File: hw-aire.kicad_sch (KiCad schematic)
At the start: 58 parts, among them J1 Conn_01x02_Pin, J2 Conn_01x02_Pin, J3 Screw_Terminal_01x12, J4 Conn_01x04_Pin, J5 Conn_01x05_Pin, K1 JRC-21F(4100), K2 JRC-21F(4100), K3 JRC-21F(4100), Q1 PMBT3904235, Q2 PMBT3904235, Q3 PMBT3904235, Q5 PMBT3904235, SW1 SW_Push, U1 HLK-2M05, U2 NCP1117-3.3_SOT223, U3 ESP-12E, U4 SHT4x, U5 BMP581

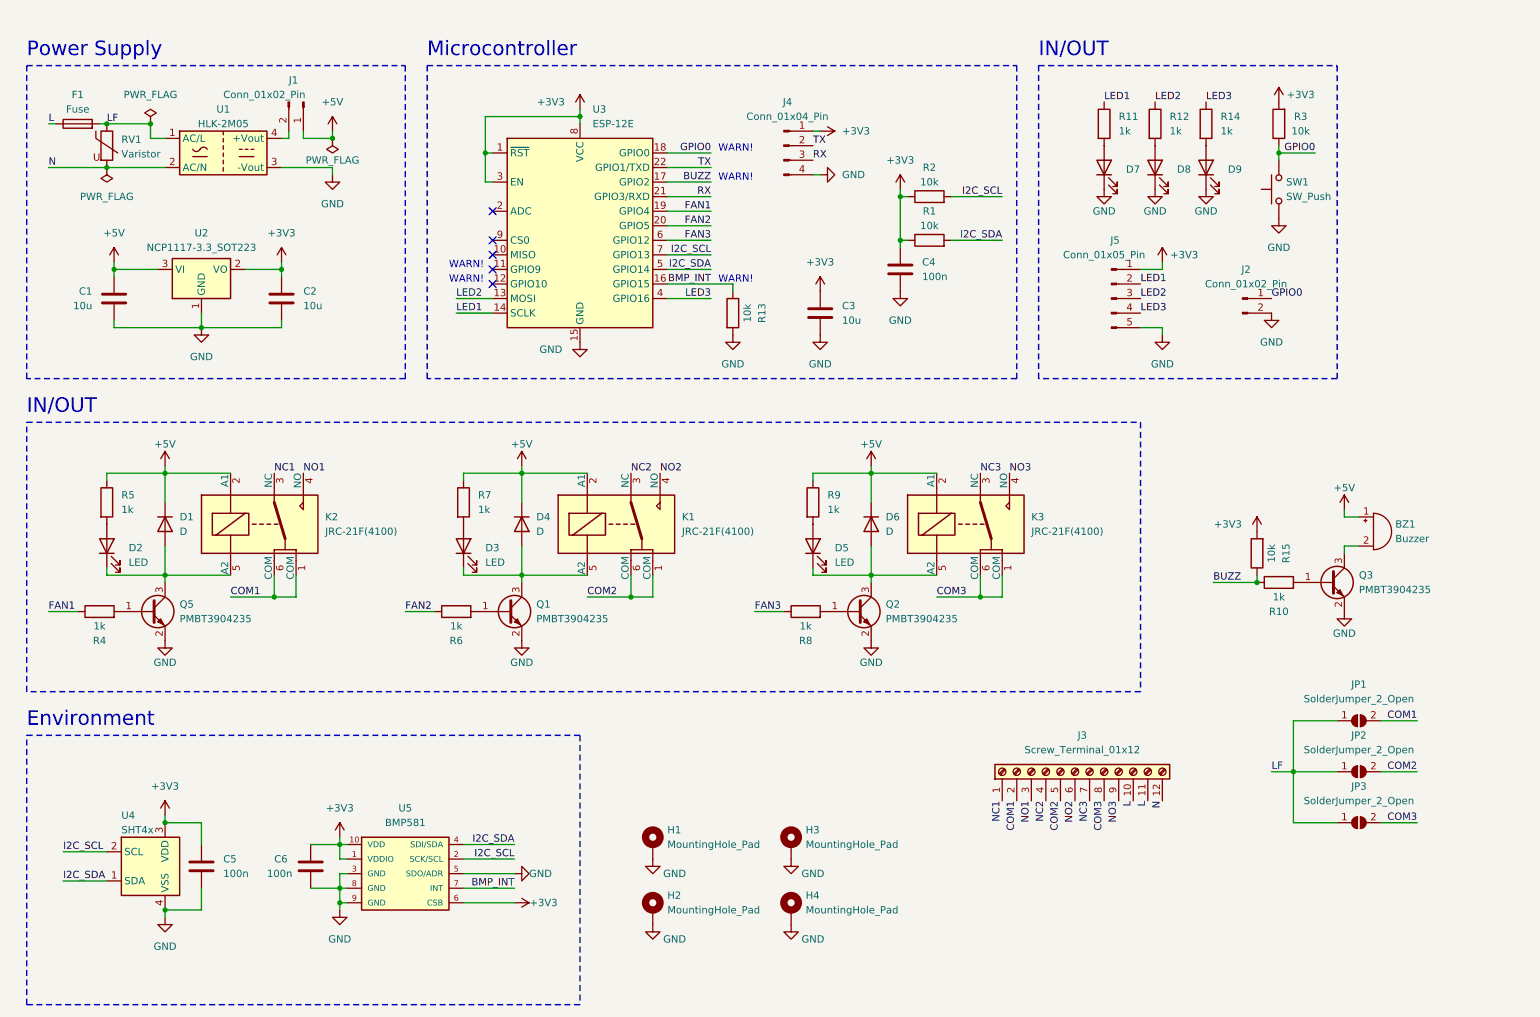
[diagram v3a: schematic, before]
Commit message: Finish routing and serigraphy. Ready to review
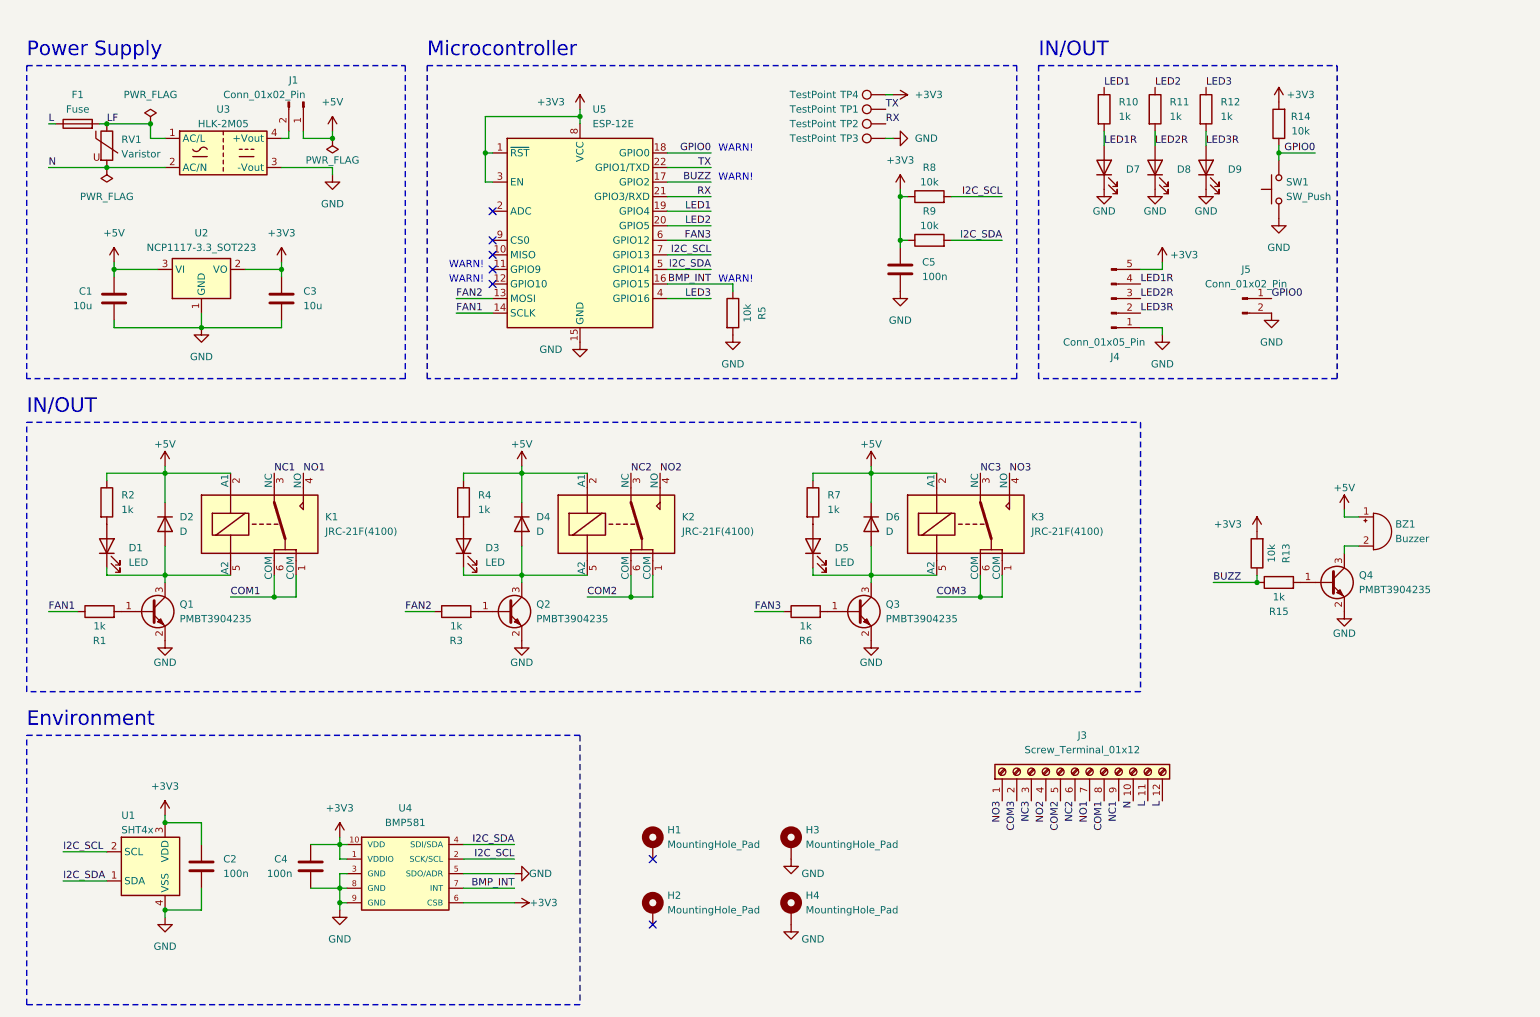
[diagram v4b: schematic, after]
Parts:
- removed C3: 10u, Capacitor_SMD:C_1206_3216Metric, symbol Device:C
- removed J4: Conn_01x04_Pin, Connector_PinHeader_2.54mm:PinHeader_1x04_P2.54mm_Vertical, symbol Connector:Conn_01x04_Pin
- removed JP1, JP2, JP3: SolderJumper_2_Open, Jumper:SolderJumper-2_P1.3mm_Open_TrianglePad1.0x1.5mm, symbol Jumper:SolderJumper_2_Open
- added TP1, TP2, TP3, TP4: TestPoint, TestPoint:TestPoint_Pad_D1.5mm, symbol Connector:TestPoint
- J4: renamed from J5; footprint Connector_PinHeader_2.54mm:PinHeader_1x05_P2.54mm_Vertical -> Connector_PinHeader_2.54mm:PinHeader_1x05_P2.54mm_Horizontal
- J5: renamed from J2; footprint Connector_PinHeader_2.54mm:PinHeader_1x02_P2.54mm_Vertical -> Connector_PinHeader_2.54mm:PinHeader_1x02_P2.54mm_Horizontal
- renumbered C5 to C2, C2 to C3, C6 to C4, C4 to C5, D2 to D1, D1 to D2, K2 to K1, K1 to K2, Q5 to Q1, Q1 to Q2, Q2 to Q3, Q3 to Q4, R4 to R1, R11 to R10, R12 to R11, R14 to R12, R15 to R13, R3 to R14, R10 to R15, R5 to R2, R6 to R3, R7 to R4, R13 to R5, R8 to R6, R9 to R7, R2 to R8, R1 to R9, U4 to U1, U1 to U3, U5 to U4, U3 to U5
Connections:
- net +3V3: now also J4.5 (Pin_5), TP4.1; no longer J4.1 (Pin_1)
- net COM1: now also J3.8 (Pin_8); no longer J3.2 (Pin_2)
- net COM3: now also J3.2 (Pin_2); no longer J3.8 (Pin_8)
- net FAN1: now also U5.14 (SCLK); no longer U5.19 (GPIO4)
- net FAN2: now also U5.13 (MOSI); no longer U5.20 (GPIO5)
- net GND: now also J4.1 (Pin_1), TP3.1; no longer H1.1, H2.1, J4.5 (Pin_5)
- net L: now also J3.12 (Pin_12); no longer J3.10 (Pin_10)
- net LED1: now also U5.19 (GPIO4); no longer J4.2 (Pin_2), U5.14 (SCLK)
- net LED2: now also U5.20 (GPIO5); no longer J4.3 (Pin_3), U5.13 (MOSI)
- net LED3: no longer J4.4 (Pin_4)
- net N: now also J3.10 (Pin_10); no longer J3.12 (Pin_12)
- net NC1: now also J3.9 (Pin_9); no longer J3.1 (Pin_1)
- net NC2: now also J3.6 (Pin_6); no longer J3.4 (Pin_4)
- net NC3: now also J3.3 (Pin_3); no longer J3.7 (Pin_7)
- net NO1: now also J3.7 (Pin_7); no longer J3.3 (Pin_3)
- net NO2: now also J3.4 (Pin_4); no longer J3.6 (Pin_6)
- net NO3: now also J3.1 (Pin_1); no longer J3.9 (Pin_9)
- net RX: now also TP2.1
- net TX: now also TP1.1
- net LED3R: now reaches D9.2 (A), R12.2
- net LED3R: now also J4.2 (Pin_2)
- net LED2R: now reaches D8.2 (A), R11.2
- net LED2R: now also J4.3 (Pin_3)
- net LED1R: now reaches D7.2 (A), R10.2
- net LED1R: now also J4.4 (Pin_4)
- no-connect marks 5 -> 7
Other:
- moved on the sheet: R10, R11, R12

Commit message: New revision, add IO expander and fix I2C GPIOs
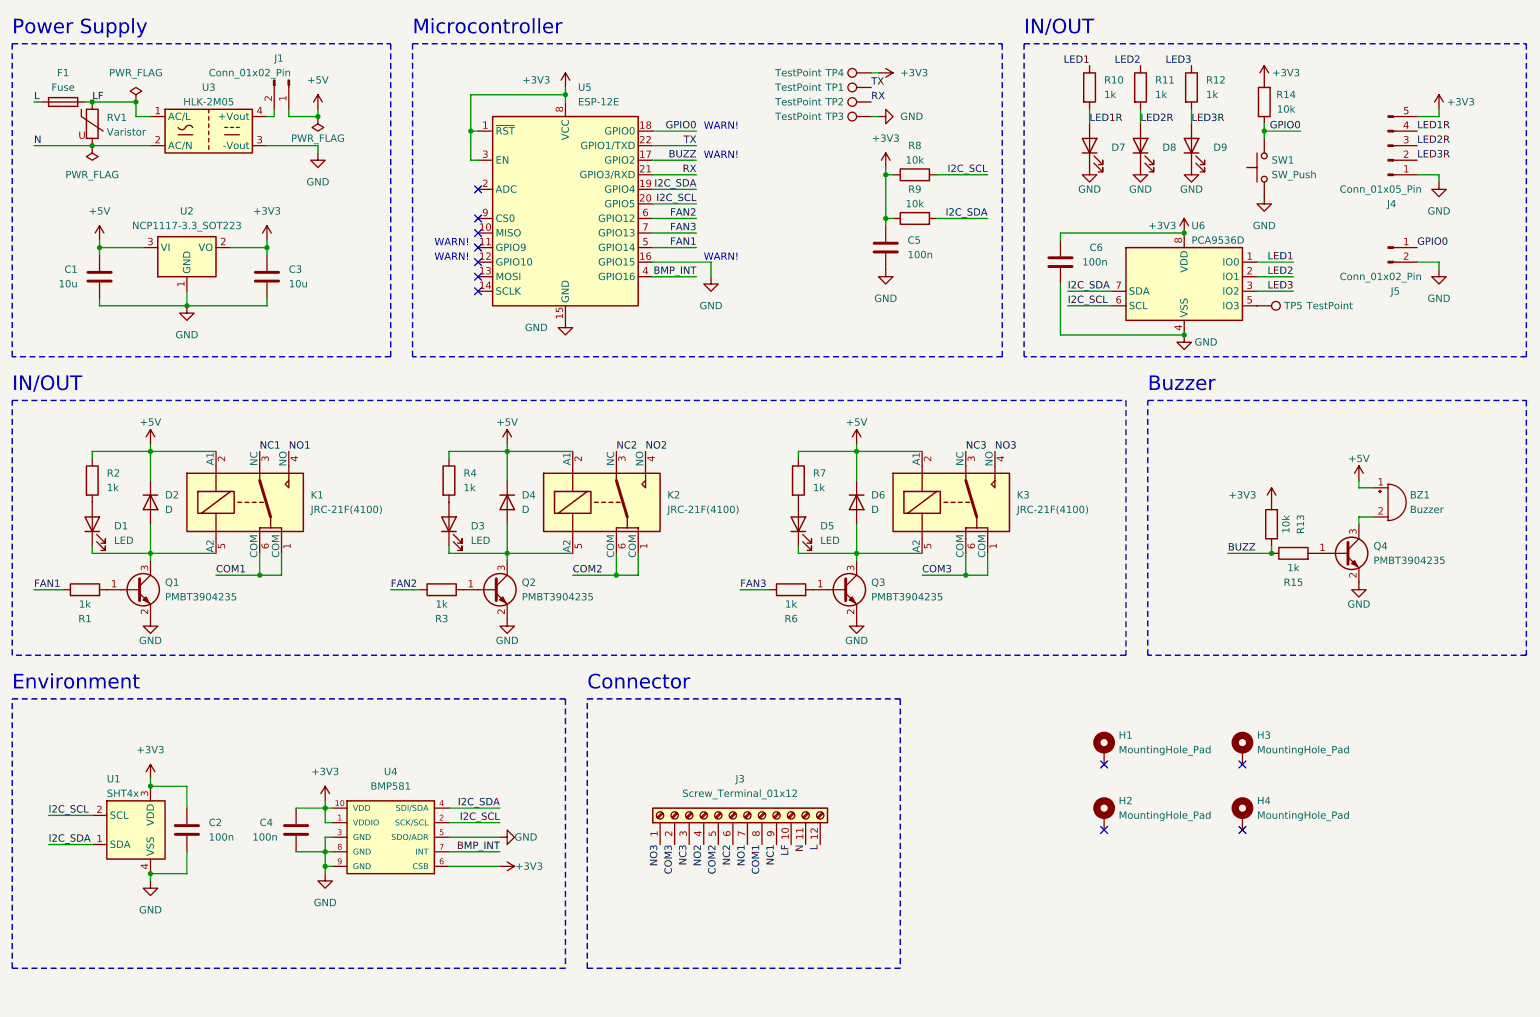
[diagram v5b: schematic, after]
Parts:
- removed R5: 10k, Resistor_SMD:R_0402_1005Metric, symbol Device:R
- added C6: 100n, Capacitor_SMD:C_0402_1005Metric, symbol Device:C
- added TP5: TestPoint, TestPoint:TestPoint_Pad_D1.5mm, symbol Connector:TestPoint
- added U6: PCA9536D, Package_SO:SOIC-8_3.9x4.9mm_P1.27mm, symbol Interface_Expansion:PCA9536D
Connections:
- net +3V3: now also C6.1, U6.8 (VDD)
- net BMP_INT: now also U5.4 (GPIO16); no longer U5.16 (GPIO15)
- net FAN1: now also U5.5 (GPIO14); no longer U5.14 (SCLK)
- net FAN2: now also U5.6 (GPIO12); no longer U5.13 (MOSI)
- net FAN3: now also U5.7 (GPIO13); no longer U5.6 (GPIO12)
- net GND: now also U5.16 (GPIO15), C6.2, U6.4 (VSS); no longer H3.1, H4.1
- net I2C_SCL: now also U5.20 (GPIO5), U6.6 (SCL); no longer U5.7 (GPIO13)
- net I2C_SDA: now also U5.19 (GPIO4), U6.7 (SDA); no longer U5.5 (GPIO14)
- net L: no longer J3.11 (Pin_11)
- net LED1: now also U6.1 (IO0); no longer U5.19 (GPIO4)
- net LED2: now also U6.2 (IO1); no longer U5.20 (GPIO5)
- net LED3: now also U6.3 (IO2); no longer U5.4 (GPIO16)
- net LF: now also J3.10 (Pin_10)
- net N: now also J3.11 (Pin_11); no longer J3.10 (Pin_10)
- new net: TP5.1, U6.5 (IO3)
- no-connect marks 7 -> 11
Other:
- note added: "Buzzer"
- note added: "Connector"
- moved on the sheet: BZ1, C1, C2, C3, C4, C5, D1, D2, D3, D4, D5, D6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
